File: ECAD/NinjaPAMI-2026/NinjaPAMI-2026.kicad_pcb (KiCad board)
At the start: 2 copper layers, 80 x 80 mm, 69 parts, among them J1 Sensor_Center, J11 Con_Batt, J13 OLED, J2 Conn_01x04, J3 Sensor_RIGHT, J4 Servo, J5 Sensor_LEFT, J6 Servo, J7 LeftMotor, J8 RightMotor, SW1 SW_SPDT, SW2 SW_Reed, SW3 SW_SPDT, U1 XIAO-HALF-HOLE-23P, U3 TMC2208_SILENTSTEPSTICK, U4 TMC2208_SILENTSTEPSTICK, U5 R-78E5.0-1.0

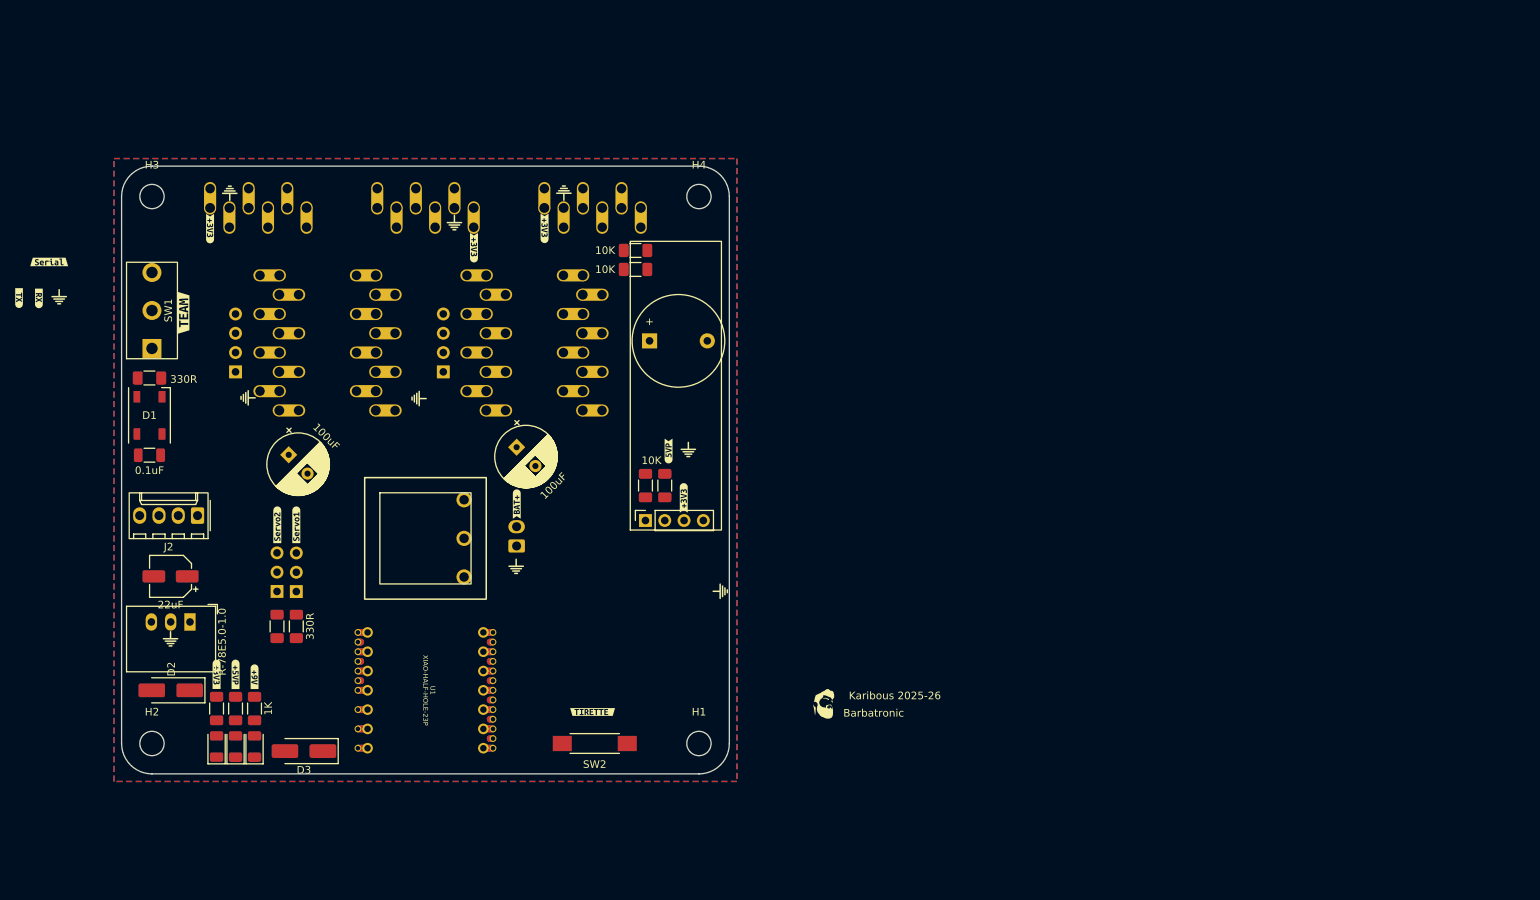
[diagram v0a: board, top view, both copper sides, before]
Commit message: change dimensions
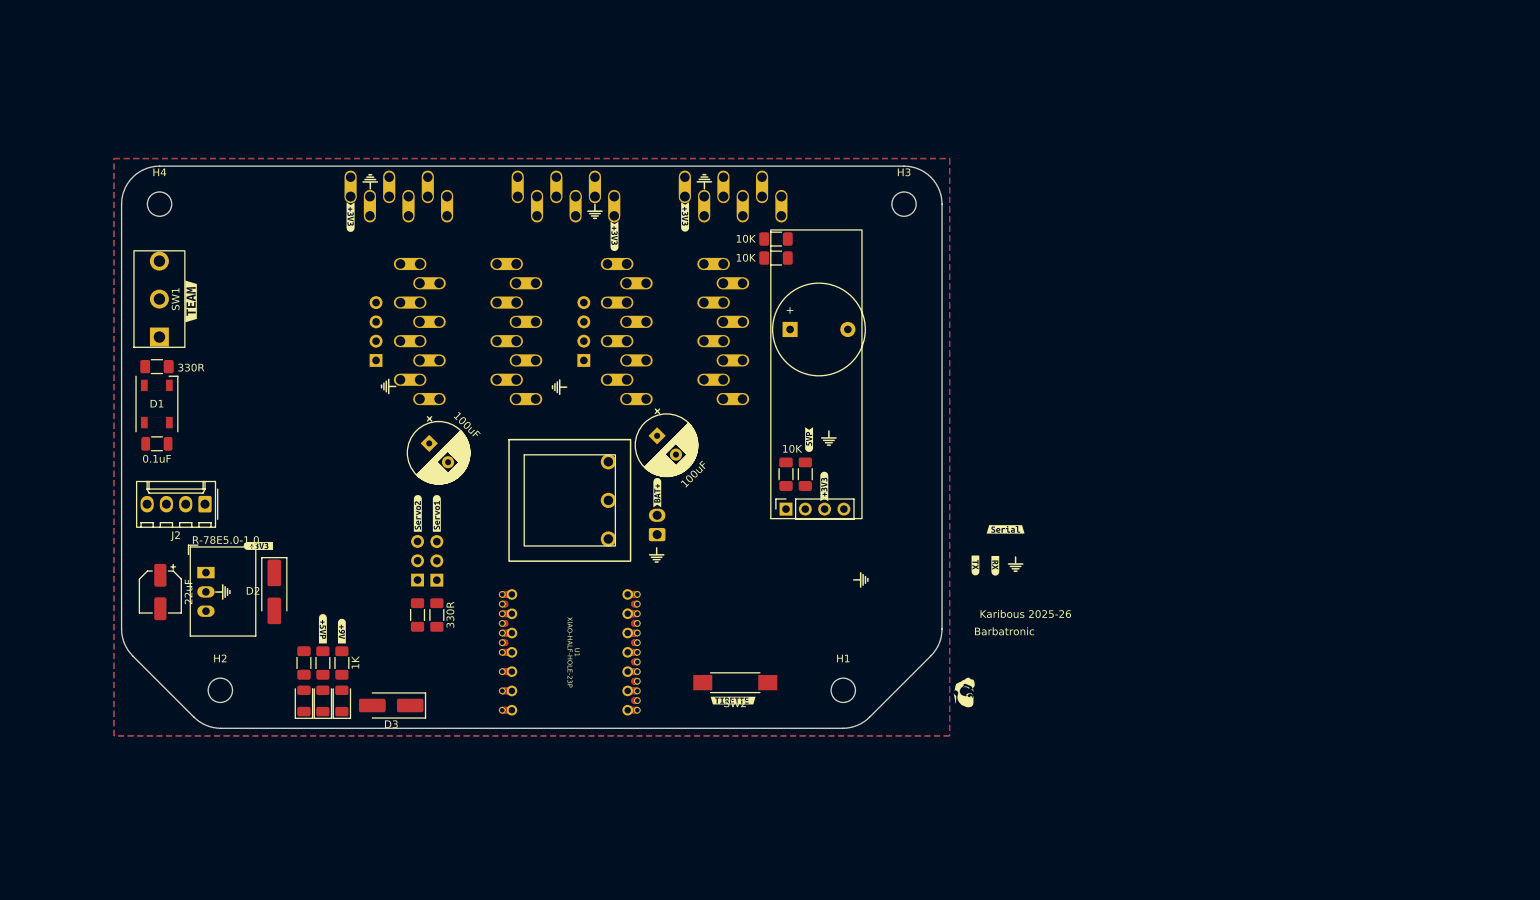
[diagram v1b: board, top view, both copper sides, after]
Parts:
- moved G*** 130.7 mm to (197.7, 117.4)
- moved kibuzzard-670C077D 130.7 mm to (196.4, 112.8)
- moved kibuzzard-670C0798 130.7 mm to (195.0, 117.6)
- moved kibuzzard-670C07A3 130.7 mm to (192.4, 117.6)
- moved H3 99.0 mm to (183.0, 70.0)
- moved H4 71.0 mm to (85.0, 70.0)
- moved H1 20.2 mm to (175.0, 134.0)
- moved SW2 20.2 mm to (160.8, 133.0)
- moved SW3 19.6 mm to (139.0, 109.0)
- moved U1 19.6 mm to (139.0, 129.0)
- moved D2 18.8 mm to (100.1, 121.0), turned to -90 degrees
- moved G*** 18.6 mm to (156.7, 67.0)
- moved G*** 18.6 mm to (190.9, 134.3)
- moved kibuzzard-670C04A5 18.6 mm to (154.2, 71.7)
- moved G*** 18.6 mm to (137.6, 94.1)
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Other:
- board size 80 x 80 mm -> 108 x 74 mm

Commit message: PAMI ninja PCB update
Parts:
- added D10: LED_Small, LED_SMD:LED_1206_3216Metric_Pad1.42x1.75mm_HandSolder, F.Cu at (262.5, 78.6)
- added D11: LED_Small, LED_SMD:LED_1206_3216Metric_Pad1.42x1.75mm_HandSolder, F.Cu at (212.6, 157.5)
- added D13: D_Small, Diode_SMD:D_SMA_Handsoldering, F.Cu at (243.9, 81.5)
- added D14: D_Small, Diode_SMD:D_SMA_Handsoldering, F.Cu at (208.7, 145.7)
- added D3: LED_Small, LED_SMD:LED_1206_3216Metric_Pad1.42x1.75mm_HandSolder, F.Cu at (246.6, 114.5)
- added D4: D_Small, Diode_SMD:D_SMA_Handsoldering, F.Cu at (242.7, 102.7)
- added D6: LED_Small, LED_SMD:LED_1206_3216Metric_Pad1.42x1.75mm_HandSolder, F.Cu at (245.6, 144.5)
- added D7: D_Small, Diode_SMD:D_SMA_Handsoldering, F.Cu at (241.7, 132.7)
- added J10: CON_EV_01, Connector_Molex:Molex_KK-254_AE-6410-02A_1x02_P2.54mm_Vertical, B.Cu at (215.0, 151.9)
- added J7: CON_EV_02, Connector_Molex:Molex_KK-254_AE-6410-02A_1x02_P2.54mm_Vertical, B.Cu at (250.0, 108.0)
- added J8: CON_EV_02, Connector_Molex:Molex_KK-254_AE-6410-02A_1x02_P2.54mm_Vertical, B.Cu at (248.0, 138.9)
- added J9: CON_PUMP_01, Connector_Molex:Molex_KK-254_AE-6410-02A_1x02_P2.54mm_Vertical, B.Cu at (258.0, 73.0)
- added JP1: SolderJumper_3_Open, Jumper:SolderJumper-3_P1.3mm_Open_RoundedPad1.0x1.5mm_NumberLabels, F.Cu at (108.9, 111.0)
- added JP2: SolderJumper_3_Open, Jumper:SolderJumper-3_P1.3mm_Open_RoundedPad1.0x1.5mm_NumberLabels, F.Cu at (250.6, 102.2)
- added JP3: SolderJumper_3_Open, Jumper:SolderJumper-3_P1.3mm_Open_RoundedPad1.0x1.5mm_NumberLabels, F.Cu at (249.6, 132.2)
- added JP4: SolderJumper_3_Open, Jumper:SolderJumper-3_P1.3mm_Open_RoundedPad1.0x1.5mm_NumberLabels, F.Cu at (109.3, 106.0)
- added JP5: SolderJumper_3_Open, Jumper:SolderJumper-3_P1.3mm_Open_RoundedPad1.0x1.5mm_NumberLabels, F.Cu at (248.7, 74.0)
- added JP6: SolderJumper_3_Open, Jumper:SolderJumper-3_P1.3mm_Open_RoundedPad1.0x1.5mm_NumberLabels, F.Cu at (216.6, 145.2)
- added Q1: AO3400A, Package_TO_SOT_SMD:SOT-23, F.Cu at (252.1, 115.0)
- added Q2: AO3400A, Package_TO_SOT_SMD:SOT-23, F.Cu at (251.1, 145.0)
- added Q3: AO3400A, Package_TO_SOT_SMD:SOT-23, F.Cu at (257.0, 81.3)
- added Q4: AO3400A, Package_TO_SOT_SMD:SOT-23, F.Cu at (218.1, 158.0)
- added R10: 270R, Resistor_SMD:R_1206_3216Metric_Pad1.30x1.75mm_HandSolder, F.Cu at (240.6, 109.9)
- added R11: 10K, Resistor_SMD:R_1206_3216Metric_Pad1.30x1.75mm_HandSolder, F.Cu at (240.6, 113.2)
- added R12: 1K, Resistor_SMD:R_1206_3216Metric_Pad1.30x1.75mm_HandSolder, F.Cu at (239.6, 136.6)
- added R13: 270R, Resistor_SMD:R_1206_3216Metric_Pad1.30x1.75mm_HandSolder, F.Cu at (239.6, 139.9)
- added R14: 10K, Resistor_SMD:R_1206_3216Metric_Pad1.30x1.75mm_HandSolder, F.Cu at (239.6, 143.2)
- added R17: 1K, Resistor_SMD:R_1206_3216Metric_Pad1.30x1.75mm_HandSolder, F.Cu at (236.6, 76.6)
- added R18: 1K, Resistor_SMD:R_1206_3216Metric_Pad1.30x1.75mm_HandSolder, F.Cu at (206.6, 149.6)
- added R19: 270R, Resistor_SMD:R_1206_3216Metric_Pad1.30x1.75mm_HandSolder, F.Cu at (242.6, 70.0)
- added R20: 270R, Resistor_SMD:R_1206_3216Metric_Pad1.30x1.75mm_HandSolder, F.Cu at (206.6, 152.9)
- added R21: 10K, Resistor_SMD:R_1206_3216Metric_Pad1.30x1.75mm_HandSolder, F.Cu at (242.6, 76.6)
- added R22: 10K, Resistor_SMD:R_1206_3216Metric_Pad1.30x1.75mm_HandSolder, F.Cu at (206.6, 156.2)
- added R9: 1K, Resistor_SMD:R_1206_3216Metric_Pad1.30x1.75mm_HandSolder, F.Cu at (240.6, 106.6)
- J13: renamed from J8; footprint Connector_PinHeader_2.54mm:PinHeader_1x04_P2.54mm_Vertical -> Connector_Molex:Molex_KK-254_AE-6410-04A_1x04_P2.54mm_Vertical
- J14: renamed from J7; footprint Connector_PinHeader_2.54mm:PinHeader_1x04_P2.54mm_Vertical -> Connector_Molex:Molex_KK-254_AE-6410-04A_1x04_P2.54mm_Vertical
- J4: renamed from J3; footprint PAMI-2025:VL53 Bottom Entry Version -> Connector_Molex:Molex_KK-254_AE-6410-06A_1x06_P2.54mm_Vertical
- J5: renamed from J1; footprint PAMI-2025:VL53 Bottom Entry Version -> Connector_Molex:Molex_KK-254_AE-6410-06A_1x06_P2.54mm_Vertical
- J6: renamed from J5; footprint PAMI-2025:VL53 Bottom Entry Version -> Connector_Molex:Molex_KK-254_AE-6410-06A_1x06_P2.54mm_Vertical
- U3, U4: value TMC2208_SILENTSTEPSTICK -> TMC2209_SILENTSTEPSTICK; footprint PAMI-2025:Step-Stick Driver Bottom Entry Version -> TMC2209_SILENTSTEPSTICK:MODULE_TMC2209_SILENTSTEPSTICK
- moved U3 39.0 mm to (115.4, 76.1), turned to 0 degrees
- moved J4 25.3 mm to (173.0, 47.0)
- moved J6 19.5 mm to (97.0, 67.9)
- moved U4 12.8 mm to (132.7, 76.1), turned to 0 degrees
- moved J5 10.3 mm to (138.5, 58.7)
- moved U2 2.00 mm to (139.0, 127.0)
- renumbered BZ2 to BZ1, C10 to C1, C11 to C2, C7 to C3, C6 to C4, D3 to D12, D4 to D2, D2 to D5, D10 to D8, D5 to D9, J11 to J1, J2 to J11, J13 to J12, J4 to J2, J6 to J3, R7 to R1, R13 to R15, R4 to R16, R10 to R2, R8 to R3, R11 to R4, R6 to R5, R12 to R6, R3 to R7, R2 to R8, SW3 to SW1, SW1 to SW3, U5 to U1, U1 to U2
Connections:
- J13 pad 1: Net-(J8-Pin_1) -> Net-(J13-Pin_1)
- J13 pad 2: Net-(J8-Pin_2) -> Net-(J13-Pin_2)
- J13 pad 3: Net-(J8-Pin_3) -> Net-(J13-Pin_3)
- J13 pad 4: Net-(J8-Pin_4) -> Net-(J13-Pin_4)
- J14 pad 1: Net-(J7-Pin_1) -> Net-(J14-Pin_1)
- J14 pad 2: Net-(J7-Pin_2) -> Net-(J14-Pin_2)
- J14 pad 3: Net-(J7-Pin_3) -> Net-(J14-Pin_3)
- J14 pad 4: Net-(J7-Pin_4) -> Net-(J14-Pin_4)
- U2 pad 7: TX -> Net-(JP1-C)
- U2 pad 8: RX -> Net-(JP4-C)
- U3 pad 1: EnDriver -> GND
- U3 pad 10: +3.3V -> RightDir
- U3 pad 11: Net-(J8-Pin_4) -> unconnected-(U3-PDN-Pad11)
- U3 pad 12: Net-(J8-Pin_3) -> unconnected-(U3-UART-Pad12)
- U3 pad 13: Net-(J8-Pin_2) -> unconnected-(U3-SPRD-Pad13)
- U3 pad 14: Net-(J8-Pin_1) -> LeftMS2
- U3 pad 15: GND -> LeftMS1
- U3 pad 16: +9V -> EnDriver
- U3 pad 2: LeftMS1 -> +3.3V
- U3 pad 3: LeftMS2 -> Net-(J13-Pin_1)
- U3 pad 4: unconnected-(U3-PDN/UART2-Pad4) -> Net-(J13-Pin_2)
- U3 pad 5: unconnected-(U3-PDN/UART1-Pad5) -> Net-(J13-Pin_3)
- U3 pad 6: (no net) -> Net-(J13-Pin_4)
- U3 pad 7: RightStep -> GND
- U3 pad 8: RightDir -> +9V
- U3 pad 9: GND -> RightStep
- U4 pad 1: EnDriver -> GND
- U4 pad 10: +3.3V -> LeftDir
- U4 pad 11: Net-(J7-Pin_4) -> unconnected-(U4-PDN-Pad11)
- U4 pad 12: Net-(J7-Pin_3) -> unconnected-(U4-UART-Pad12)
- U4 pad 13: Net-(J7-Pin_2) -> unconnected-(U4-SPRD-Pad13)
- U4 pad 14: Net-(J7-Pin_1) -> LeftMS2
- U4 pad 15: GND -> LeftMS1
- U4 pad 16: +9V -> EnDriver
- U4 pad 2: LeftMS1 -> +3.3V
- U4 pad 3: LeftMS2 -> Net-(J14-Pin_1)
- U4 pad 4: unconnected-(U4-PDN/UART2-Pad4)_1 -> Net-(J14-Pin_2)
- U4 pad 5: unconnected-(U4-PDN/UART1-Pad5)_1 -> Net-(J14-Pin_3)
- U4 pad 6: (no net) -> Net-(J14-Pin_4)
- U4 pad 7: LeftStep -> GND
- U4 pad 8: LeftDir -> +9V
- U4 pad 9: GND -> LeftStep
